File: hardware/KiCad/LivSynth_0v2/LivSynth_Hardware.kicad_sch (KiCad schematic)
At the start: 0 parts

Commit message: Before fixing HW issues
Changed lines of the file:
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@@
     (effects (font (size 1.27 1.27)) (justify left bottom))
   )
-  (text "Todos:\n - Done: Use GND + 3.3V copper pours (\"power paddles\") around voltage regulator section (https://www.youtube.com/watch?v=aVUqaB0IMh4 1:29:30)\n   - Clearance 0.3, Minimum width 0.25\n - Soldering holes for 12BH6211-GR too big, 1mm sufficient\n - Make D1 Schottky Diode\n - Increase C26 -> 1u\n - Redesign EG LED schematic\n - Invert RV3 (VCF Cutoff) and RV7 (VCF Resonance) connection (left: close/none, right: open/full)\n - Invert RV11 (VCA Bias) connection (left: close, right: open)\n - Reference EG -> VGND!\n - Check EG timing: Decay should be slower\n - Apply attenuverters to the EG modulation paths\n - Add switch labels to front side\n - How to make the synth fully silent?\n - Add some debug pin to MCU\n - Add SloBlo icon\n - Add Schottky Diode from VBUS to LM1117 input, remove R56\n - Add MCU Debug pins\n - DFU only FS mode compatible. Reroute USB to PA11 and PA12\n - Connect unused SR inputs to GND\n - HC165: pull unused inputs to GND\n - add MCU reset button (pull to GND)\n - set SPI to Full-Duplex (add MOSI pin, left unused)\n - Tempo knob needs inversion\n - Pitch know needs inversion\n"
+  (text "Todos:\n - Done: Use GND + 3.3V copper pours (\"power paddles\") around voltage regulator section (https://www.youtube.com/watch?v=aVUqaB0IMh4 1:29:30)\n   - Clearance 0.3, Minimum width 0.25\n - Soldering holes for 12BH6211-GR too big, 1mm sufficient\n - Make D1 Schottky Diode\n - Increase C26 -> 1u\n - Redesign EG LED schematic\n - Invert RV3 (VCF Cutoff) and RV7 (VCF Resonance) connection (left: close/none, right: open/full)\n - Invert RV11 (VCA Bias) connection (left: close, right: open)\n - Reference EG -> VGND!\n - Check EG timing: Decay should be slower\n - Apply attenuverters to the EG modulation paths\n - Add switch labels to front side\n - How to make the synth fully silent?\n - Add some debug pin to MCU\n - Add SloBlo icon\n - Add Schottky Diode from VBUS to LM1117 input, remove R56\n - Add MCU Debug pins\n - DFU only FS mode compatible. Reroute USB to PA11 and PA12\n - Connect unused SR inputs to GND\n - HC165: pull unused inputs to GND\n - add MCU reset button (pull to GND)\n - set SPI to Full-Duplex (add MOSI pin, left unused)\n - Tempo knob needs inversion\n - Pitch know needs inversion\n - EG: Connect R72 with D7 directly, otherwise looping does not work\n - R52 -> 2K\n - C26 -> 10uF\n - "
     (at 120.65 182.88 0)
     (effects (font (size 1.27 1.27)) (justify left bottom))
@@
     )
     (path "/5bba0015-9baa-48b8-b961-e7169713a149/5bcd4196-1721-40ea-bafe-95ac02171038"
-      (reference "R34") (unit 1) (value "20K") (footprint "Resistor_THT:R_Axial_DIN0207_L6.3mm_D2.5mm_P7.62mm_Horizontal")
+      (reference "R34") (unit 1) (value "4K7") (footprint "Resistor_THT:R_Axial_DIN0207_L6.3mm_D2.5mm_P7.62mm_Horizontal")
     )
     (path "/a0830201-d177-4d04-9261-1bfa7e92760e/f8eadc45-80ee-4534-a705-4c60e25b1d15"

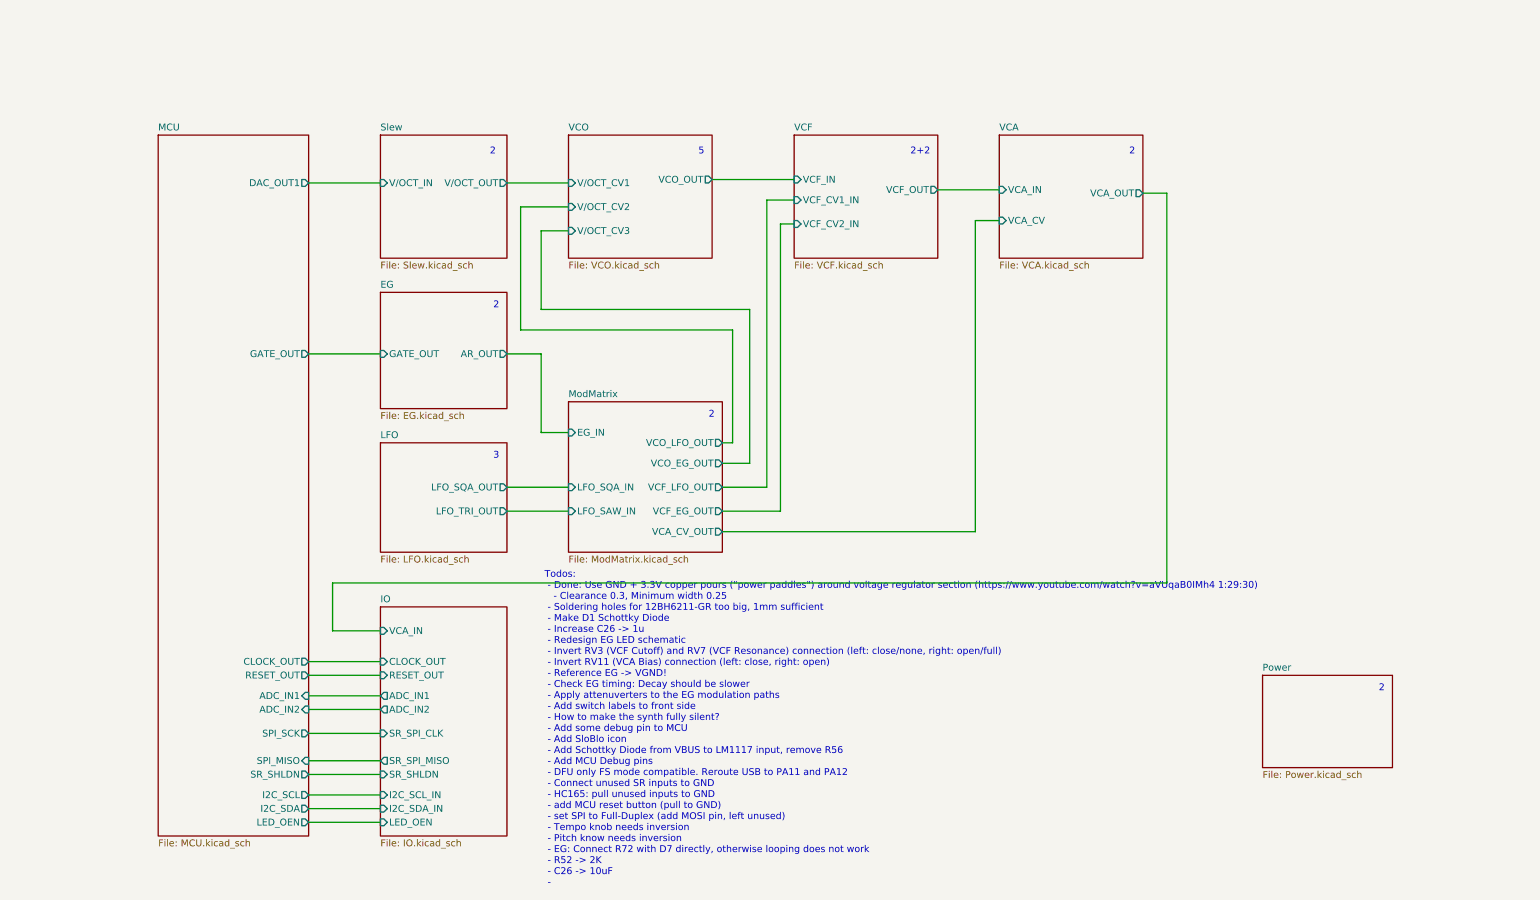
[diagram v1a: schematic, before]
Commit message: Analog redesign:  - Power: Add voltage and current test points  - MCU: use PA11/PA12 for USB DFU interface  - MCU: add NRST reset switch  - Slew: increase portamento cap  - VCO: invert trim pots  - VCF: let resonance kick in earlier  - VCF: invert pots  - VCA: invert trim pot  - EG: full redesign, properly referencing VGND now  - LFO: R61 = 51K  - ModMatrix: add EG attenuverters  - IO: invert pots  - IO: limit output gain for 1W speaker  - IO: connect BTN_SHIFT in gap free order to SR
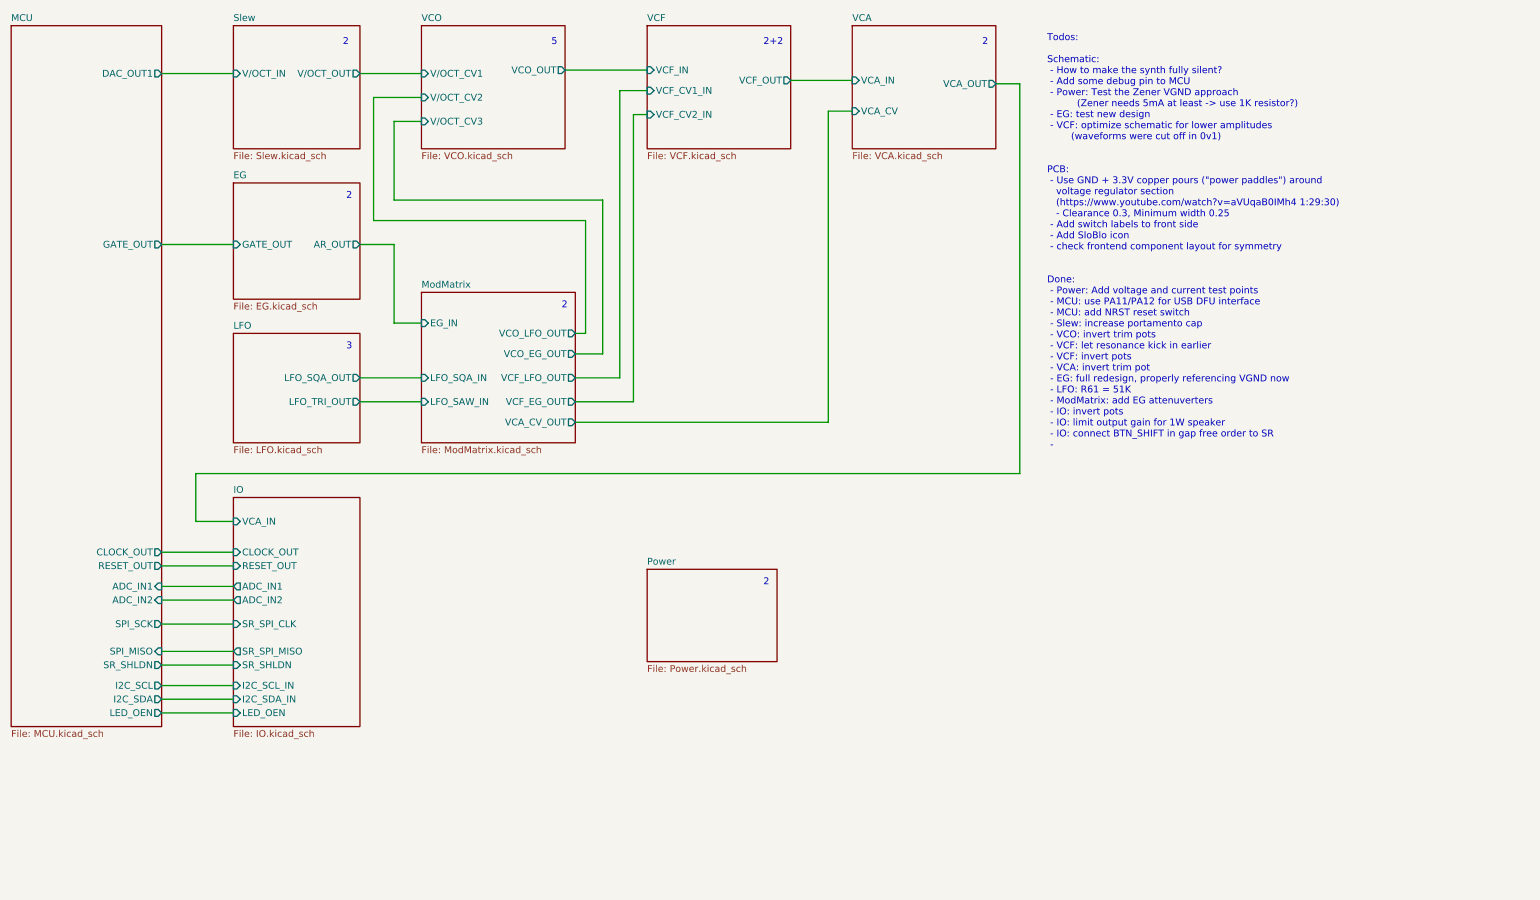
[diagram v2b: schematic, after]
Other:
- note added: "Todos: Schematic: - How to make the synth fully silent? - Add some debug pin to MCU - Power: Test the Zener VGND approach (Zener needs 5mA at least -> use 1K resistor?) - EG: test new design - VCF: optimize schematic for lower amplitudes (waveforms were cut off in 0v1) PCB: - Use GND + 3.3V copper pours ("power paddles") around voltage regulator section (https://www.youtube.com/watch?v=aVUqaB0IMh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"
- note removed: "Todos: - Done: Use GND + 3.3V copper pours ("power paddles") around voltage regulator section (https://www.youtube.com/watch?v=aVUqaB0IMh4 1:29:30) - Clearance 0.3, Minimum width 0.25 - Soldering holes for 12BH6211-GR too big, 1mm sufficient - Make D1 Schottky Diode - Increase C26 -> 1u - Redesign EG LED schematic - Invert RV3 (VCF Cutoff) and RV7 (VCF Resonance) connection (left: close/none, rig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"

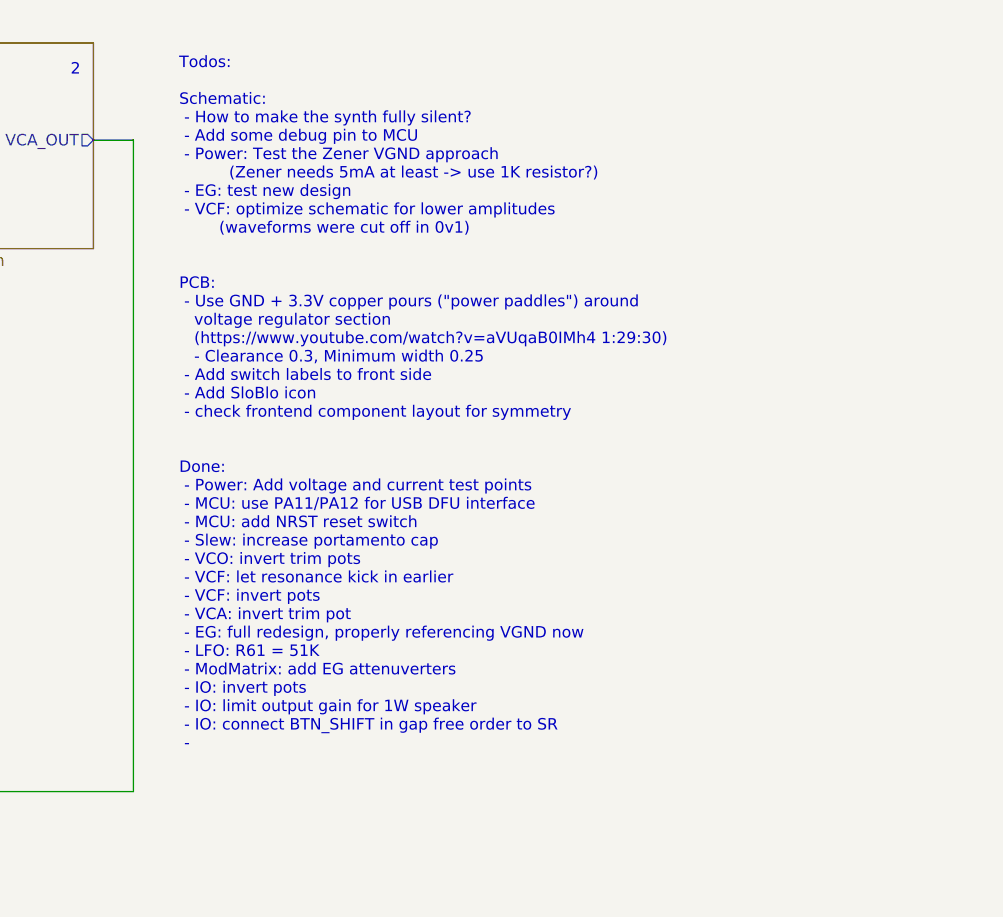
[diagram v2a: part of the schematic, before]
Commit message: Analog Redesign:  - Power: Build ververse polarity protection using P-Mosfet and Zener Diode      - (https://www.youtube.com/watch?v=Ltx4vovY5Z4 - 1:28)  - Power: Build adjustable buck regulator for 8-9V stable voltage source  - PCB: Add location for order number ("JLCJLCJLCJLC")  - General: Add Tooling Holes for PCB assembly  - PCB: check frontend component layout for symmetry  - VCF: fix sound issues  - PCB: Add SloBlo icon  - PCB: Add switch labels to front side  - EG: test new design  - MCU: Add some debug pins
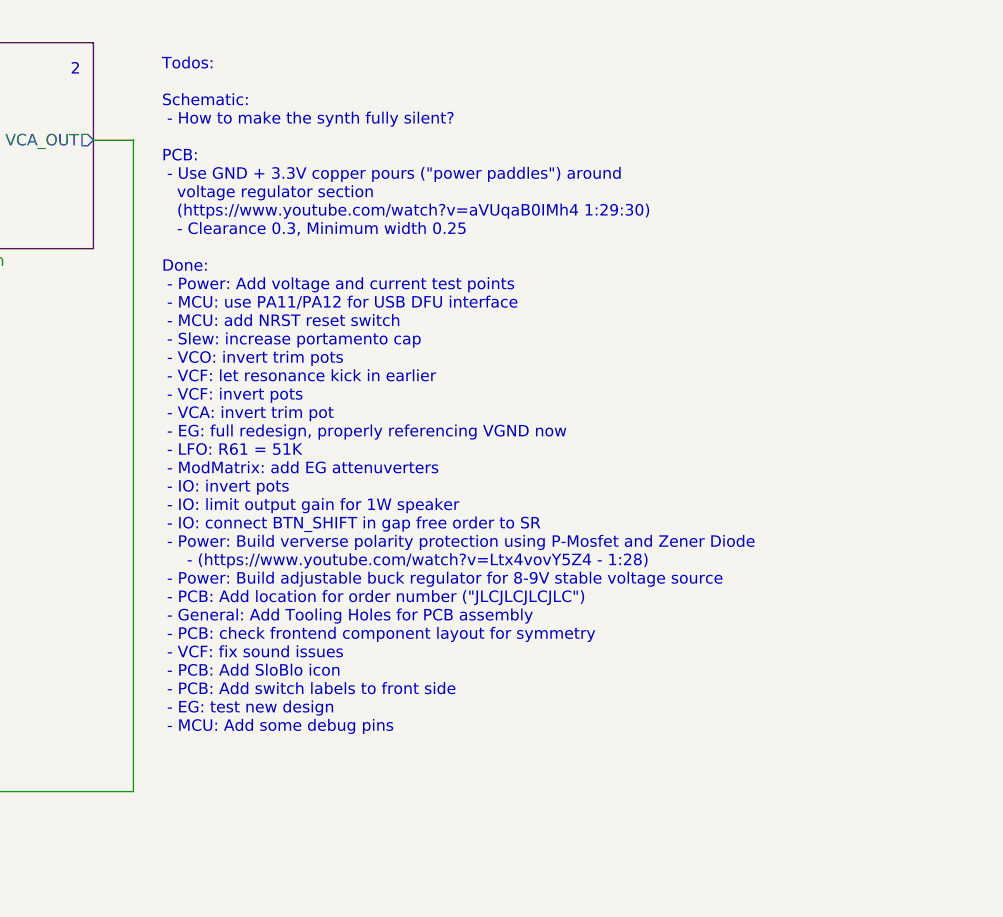
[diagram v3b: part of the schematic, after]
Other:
- note added: "Todos: Schematic: - How to make the synth fully silent? PCB: - Use GND + 3.3V copper pours ("power paddles") around voltage regulator section (https://www.youtube.com/watch?v=aVUqaB0IMh4 1:29:30) - Clearance 0.3, Minimum width 0.25 Done: - Power: Add voltage and current test points - MCU: use PA11/PA12 for USB DFU interface - MCU: add NRST reset switch - Slew: increase portamento cap - VCO: inver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"
- note removed: "Todos: Schematic: - How to make the synth fully silent? - Add some debug pin to MCU - Power: Test the Zener VGND approach (Zener needs 5mA at least -> use 1K resistor?) - EG: test new design - VCF: optimize schematic for lower amplitudes (waveforms were cut off in 0v1) PCB: - Use GND + 3.3V copper pours ("power paddles") around voltage regulator section (https://www.youtube.com/watch?v=aVUqaB0IMh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"

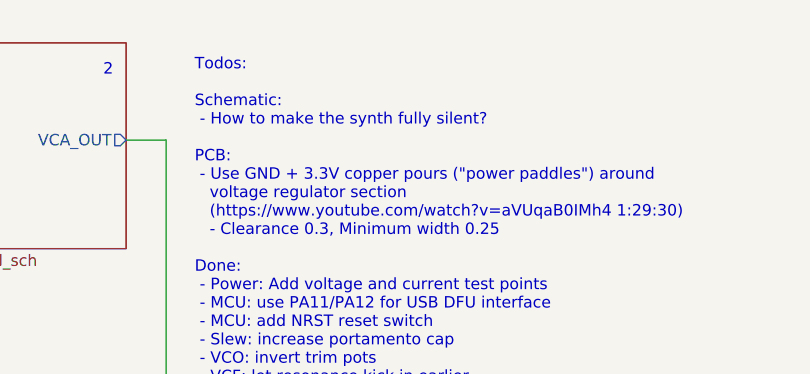
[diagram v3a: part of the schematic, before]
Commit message: Keep selected note always active for editing Fix annoying gate issue
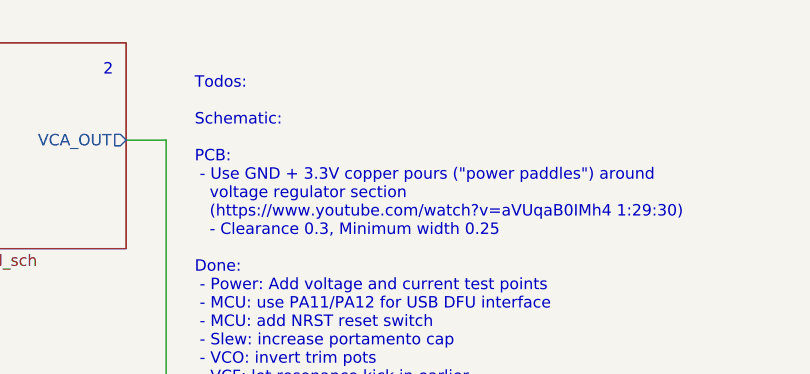
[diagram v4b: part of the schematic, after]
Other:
- note added: "Todos: Schematic: PCB: - Use GND + 3.3V copper pours ("power paddles") around voltage regulator section (https://www.youtube.com/watch?v=aVUqaB0IMh4 1:29:30) - Clearance 0.3, Minimum width 0.25 Done: - Power: Add voltage and current test points - MCU: use PA11/PA12 for USB DFU interface - MCU: add NRST reset switch - Slew: increase portamento cap - VCO: invert trim pots - VCF: let resonance kick 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"
- note removed: "Todos: Schematic: - How to make the synth fully silent? PCB: - Use GND + 3.3V copper pours ("power paddles") around voltage regulator section (https://www.youtube.com/watch?v=aVUqaB0IMh4 1:29:30) - Clearance 0.3, Minimum width 0.25 Done: - Power: Add voltage and current test points - MCU: use PA11/PA12 for USB DFU interface - MCU: add NRST reset switch - Slew: increase portamento cap - VCO: inver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"
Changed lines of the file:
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@@
     (effects (font (size 1.27 1.27)) (justify left bottom))
   )
-  (text "Todos:\n\nSchematic:\n - How to make the synth fully silent?\n\nPCB:\n - Use GND + 3.3V copper pours (\"power paddles\") around\n   voltage regulator section\n   (https://www.youtube.com/watch?v=aVUqaB0IMh4 1:29:30)\n   - Clearance 0.3, Minimum width 0.25\n\nDone:\n - Power: Add voltage and current test points\n - MCU: use PA11/PA12 for USB DFU interface\n - MCU: add NRST reset switch\n - Slew: increase portamento cap\n - VCO: invert trim pots\n - VCF: let resonance kick in earlier\n - VCF: invert pots\n - VCA: invert trim pot\n - EG: full redesign, properly referencing VGND now\n - LFO: R61 = 51K\n - ModMatrix: add EG attenuverters\n - IO: invert pots\n - IO: limit output gain for 1W speaker\n - IO: connect BTN_SHIFT in gap free order to SR\n - Power: Build ververse polarity protection using P-Mosfet and Zener Diode\n     - (https://www.youtube.com/watch?v=Ltx4vovY5Z4 - 1:28)\n - Power: Build adjustable buck regulator for 8-9V stable voltage source\n - PCB: Add location for order number (\"JLCJLCJLCJLC\")\n - General: Add Tooling Holes for PCB assembly\n - PCB: check frontend component layout for symmetry\n - VCF: fix sound issues\n - PCB: Add SloBlo icon\n - PCB: Add switch labels to front side\n - EG: test new design\n - MCU: Add some debug pins"
+  (text "Todos:\n\nSchematic:\n\nPCB:\n - Use GND + 3.3V copper pours (\"power paddles\") around\n   voltage regulator section\n   (https://www.youtube.com/watch?v=aVUqaB0IMh4 1:29:30)\n   - Clearance 0.3, Minimum width 0.25\n\nDone:\n - Power: Add voltage and current test points\n - MCU: use PA11/PA12 for USB DFU interface\n - MCU: add NRST reset switch\n - Slew: increase portamento cap\n - VCO: invert trim pots\n - VCF: let resonance kick in earlier\n - VCF: invert pots\n - VCA: invert trim pot\n - EG: full redesign, properly referencing VGND now\n - LFO: R61 = 51K\n - ModMatrix: add EG attenuverters\n - IO: invert pots\n - IO: limit output gain for 1W speaker\n - IO: connect BTN_SHIFT in gap free order to SR\n - Power: Build ververse polarity protection using P-Mosfet and Zener Diode\n     - (https://www.youtube.com/watch?v=Ltx4vovY5Z4 - 1:28)\n - Power: Build adjustable buck regulator for 8-9V stable voltage source\n - PCB: Add location for order number (\"JLCJLCJLCJLC\")\n - General: Add Tooling Holes for PCB assembly\n - PCB: check frontend component layout for symmetry\n - VCF: fix sound issues\n - PCB: Add SloBlo icon\n - PCB: Add switch labels to front side\n - EG: test new design\n - MCU: Add some debug pins"
     (at 212.09 99.695 0)
     (effects (font (size 1.27 1.27)) (justify left bottom))

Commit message: progress 2023-01-21
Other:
- sheet MCU ports: added SR_SPI_MISO, SR_SPI_SCK; removed SPI_MISO, SPI_SCK
- note added: "OPA 1xU3, 1xU8"
- note added: "OPA 2xU1"
- note added: "OPA 2xU3"
- note added: "OPA 2xU6"
- note added: "OPA 2xU6 OTA 2x"
- note added: "OPA 3xU8"
- note added: "OPA 4xU4, 1xU3"
- note removed: "2"
- note removed: "2+2"
- note removed: "3"
- note removed: "5"
